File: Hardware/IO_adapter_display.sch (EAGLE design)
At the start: 26 parts, among them J0 2.1MMJACKSMT, Y1 32Khz

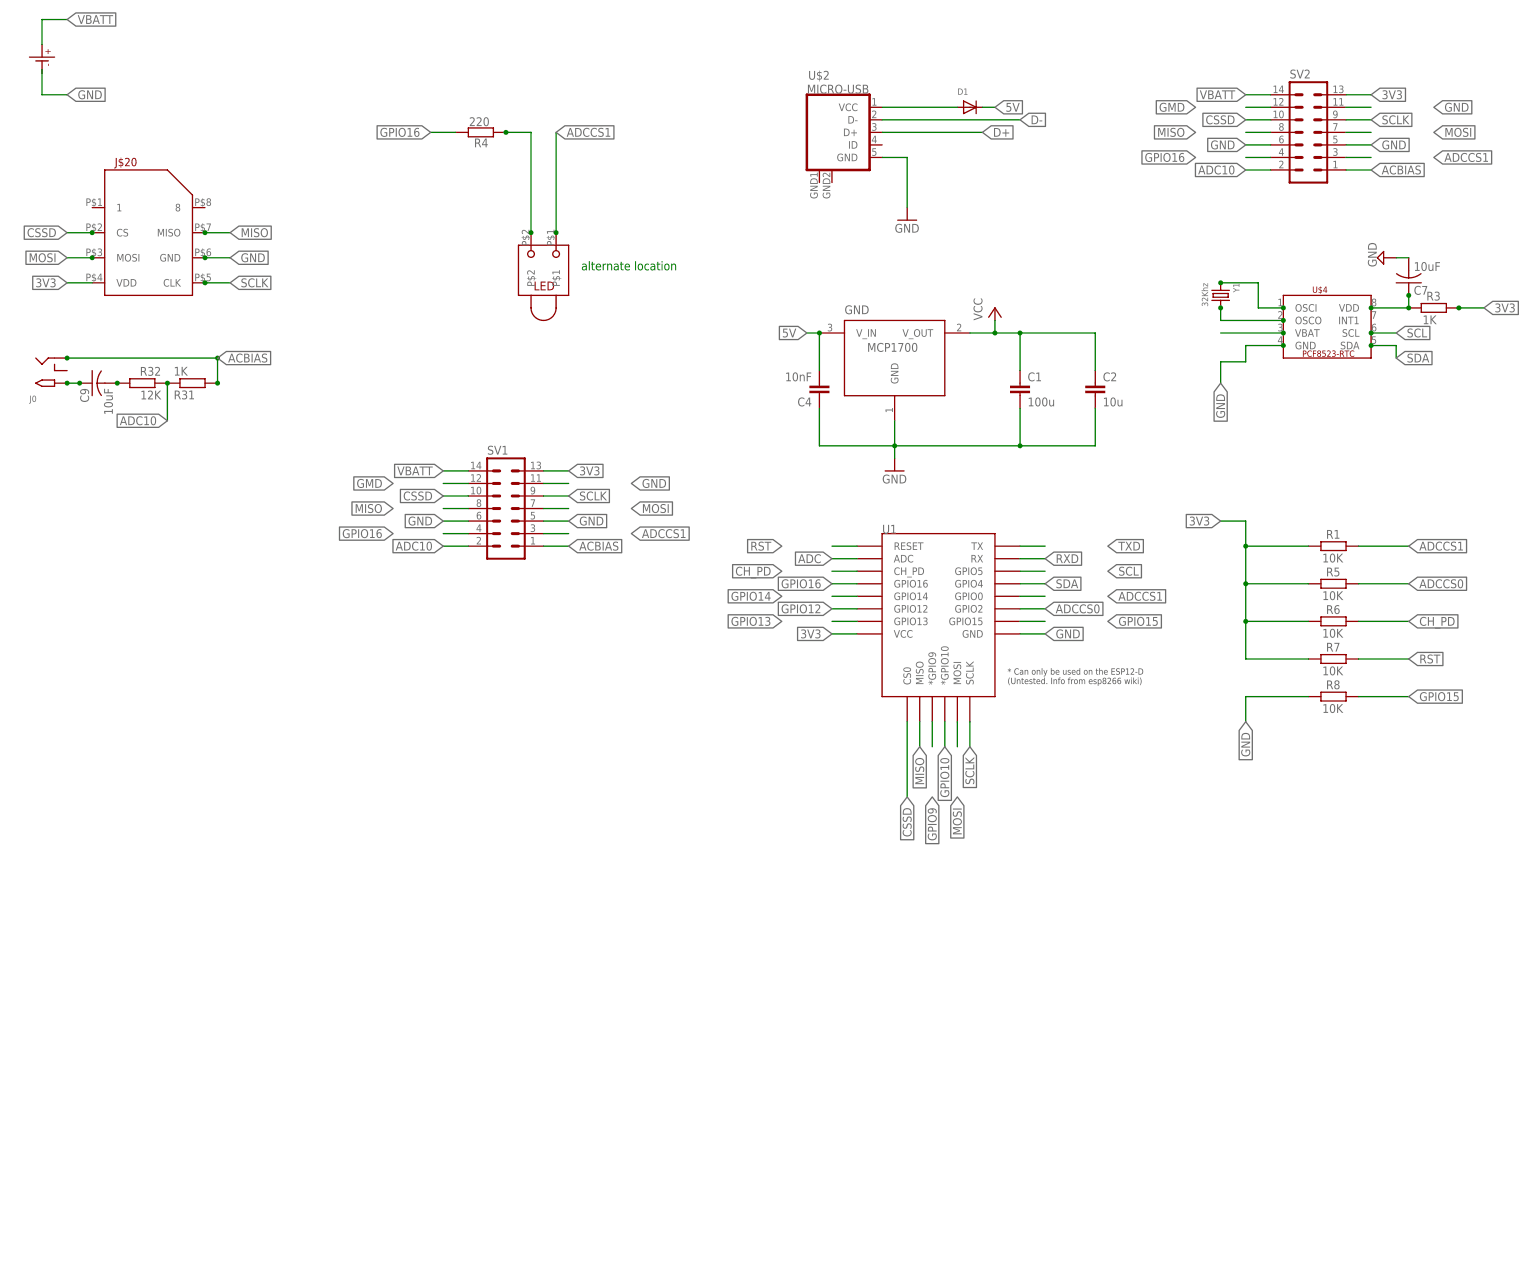
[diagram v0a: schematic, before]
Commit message: beginning to add a 2.2" TFT display
not quite sure about the mechanical layout yet.
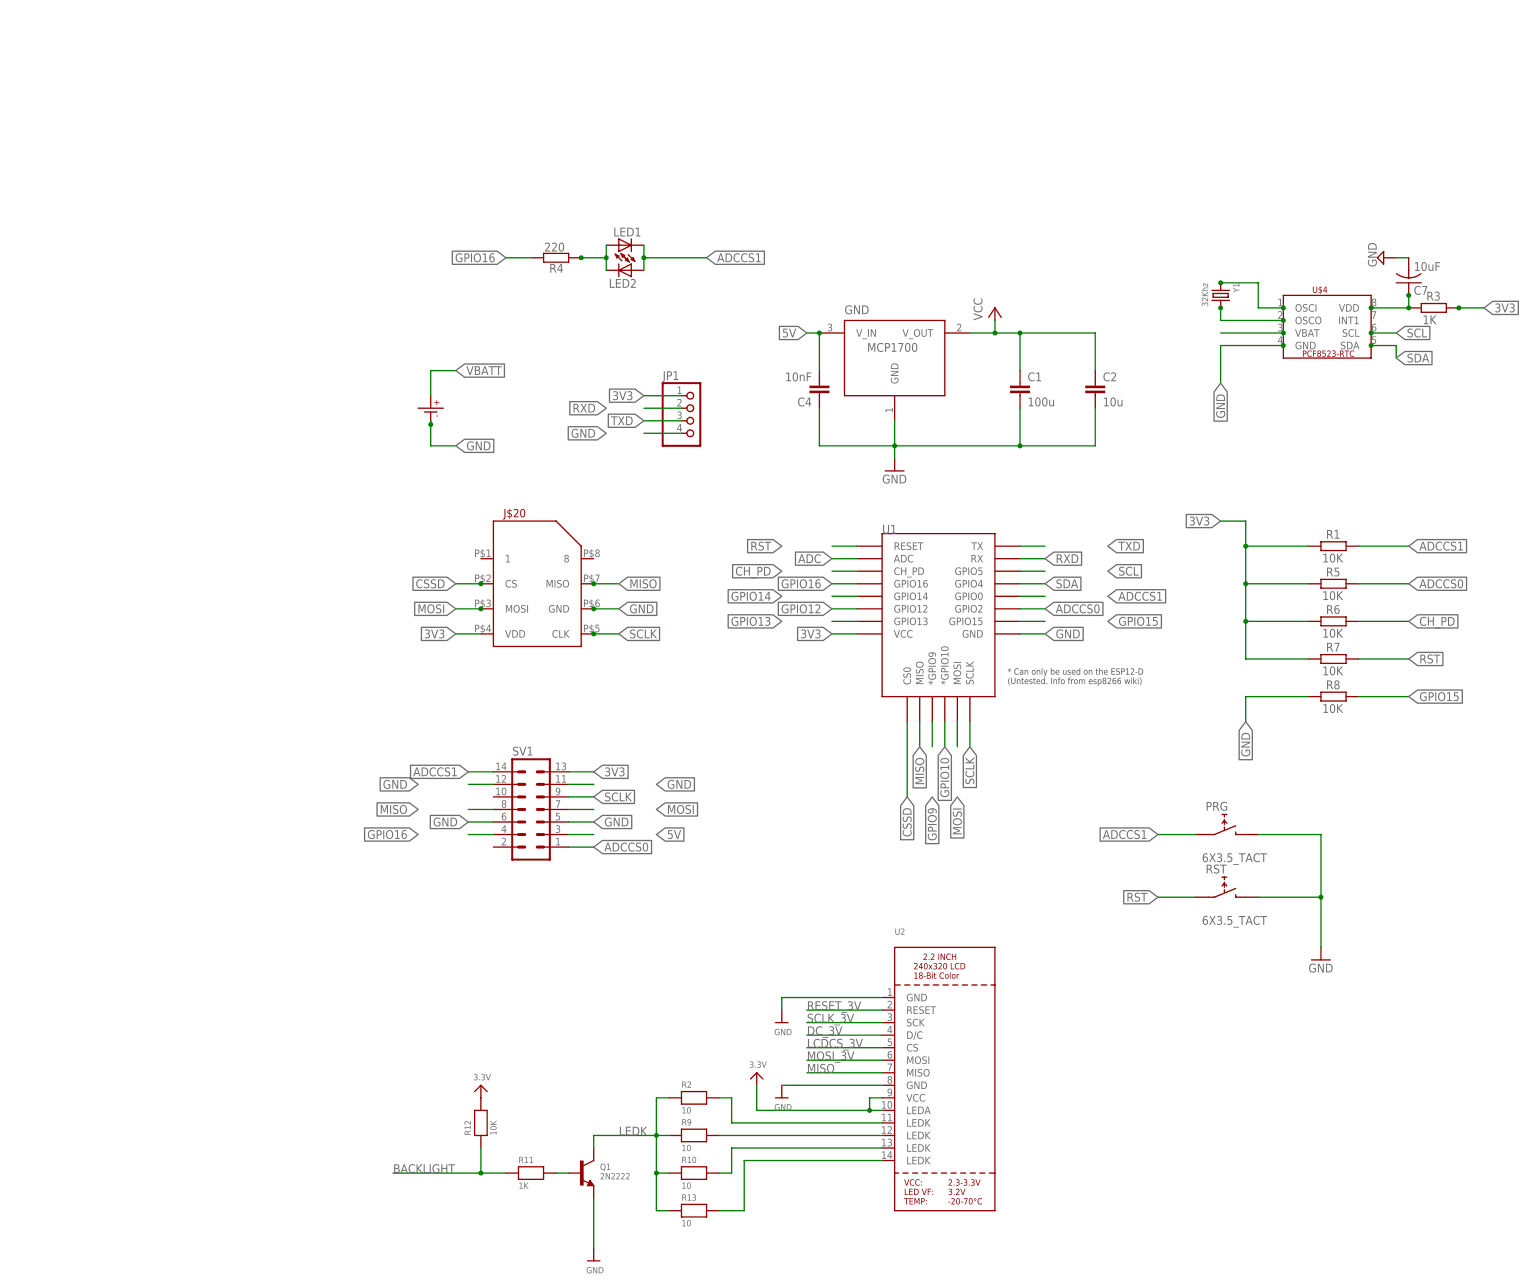
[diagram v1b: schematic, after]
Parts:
- removed C9: 10uF, adafruit:C-USC0805
- removed D1: (no value), adafruit:DIODESOD-323F
- removed J0: 2.1MMJACKSMT, IotaWatt_parts:2.1MMJACKSMT
- removed R31: 1K, resistor:R-EU_R0805
- removed R32: 12K, resistor:R-EU_R0805
- removed SV2: (no value), con-lstb:MA07-2
- removed U$2: MICRO-USB, microusb (1):MICRO-USB
- removed U$23: LED_RT_TRH, IotaWatt_parts:LED_RT_TRH
- added JP1: (no value), pinhead:PINHD-1X4
- added LED1, LED2: (no value), adafruit:LEDCHIPLED_0805
- added PRG, RST: 6X3.5_TACT, tactile_switch:6X3.5_TACT
- added Q1: 2N2222, microbuilder:TRANSISTOR_NPNWIDE
- added R10, R13, R2, R9: 10, microbuilder:RESISTOR_0805MP
- added R11: 1K, microbuilder:RESISTOR_0805MP
- added R12: 10K, microbuilder:RESISTOR_0805MP
- added U2: (no value), microbuilder:DISP_LCD_TM022HDH26
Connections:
- removed net 5VUSB: D1.A, U$2.VCC
- removed net ACBIAS: J0.RING, R31.2, SV1.1, SV2.1
- removed net ADC10: R31.1, R32.1, SV1.2, SV2.2
- removed net D+: U$2.D+
- removed net D-: U$2.D-
- removed net GMD: SV1.12, SV2.12
- removed net N$17: C9.2, R32.2
- removed net N$27: C9.1, J0.TIP
- removed net VBATT1: U$4.VBAT
- new net 3.3V: R12.2, U2.LEDA, U2.VCC
- new net BACKLIGHT: R11.1, R12.1
- new net DC_3V: U2.D/C
- new net LCDCS_3V: U2.CS
- new net LEDK: Q1.C, R10.1, R13.1, R2.1, R9.1
- new net MOSI_3V: U2.MOSI
- new net N$2: R2.2, U2.LEDK@1
- new net N$3: R9.2, U2.LEDK@2
- new net N$4: R10.2, U2.LEDK@3
- new net N$5: Q1.B, R11.2
- new net N$6: R13.2, U2.LEDK@4
- new net RESET_3V: U2.RESET
- new net SCLK_3V: U2.SCK
- net 3V3: now also JP1.1; no longer SV2.13
- net 5V: now also SV1.3; no longer D1.C
- net ADCCS0: now also SV1.1
- net ADCCS1: now also LED1.C, LED2.A, PRG.1, SV1.14; no longer SV1.3, SV2.3, U$23.P$1
- net CSSD: no longer SV1.10, SV2.10
- net GND: now also JP1.4, PRG.2, Q1.E, RST.2, SV1.12, U$1.P$-, U2.GND@1, U2.GND@2; no longer SV2.11, SV2.5, SV2.6, U$2.GND
- net GPIO16: no longer SV2.4
- net MISO: now also U2.MISO; no longer SV2.8
- net MOSI: no longer SV2.7
- net N$8: now also LED1.A, LED2.C; no longer U$23.P$2
- net RST: now also RST.1
- net RXD: now also JP1.2
- net SCLK: no longer SV2.9
- net TXD: now also JP1.3
- net VBATT: now also U$4.VBAT; no longer SV1.14, SV2.14
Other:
- note removed: "alternate location"
- moved on the sheet: J$20, R4, SV1
